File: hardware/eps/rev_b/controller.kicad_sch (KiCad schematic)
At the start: 11 parts, among them J100 SWD_ACCESS_LOGICAL, U100 STM32G0B1KET6N, Y100 ECS-3225MV-160-BN-TR

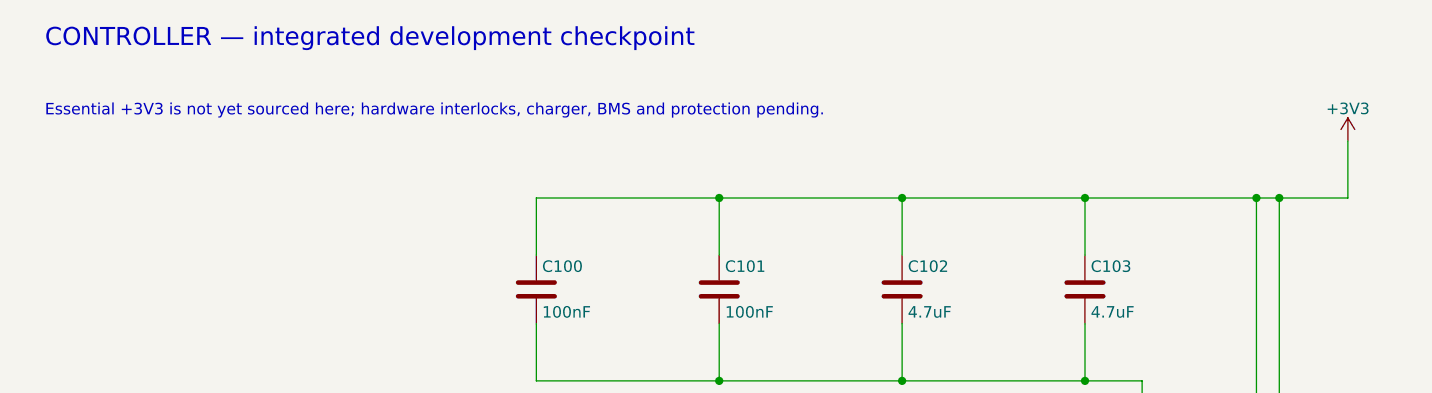
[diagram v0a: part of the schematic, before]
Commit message: Integrate essential 3V3 buck into EPS Rev B
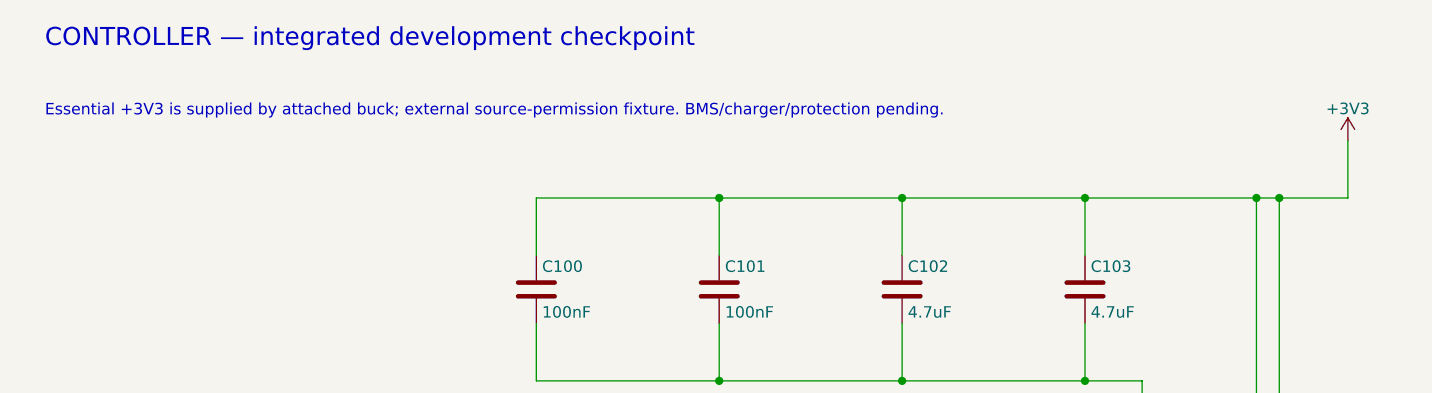
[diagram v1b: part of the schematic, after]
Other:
- note added: "Essential +3V3 is supplied by attached buck; external source-permission fixture. BMS/charger/protection pending."
- note removed: "Essential +3V3 is not yet sourced here; hardware interlocks, charger, BMS and protection pending."
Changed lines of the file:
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@@
     (effects (font (size 2 2)) (justify left bottom))
-  )
-  (text "Essential +3V3 is not yet sourced here; hardware interlocks, charger, BMS and protection pending."
-    (at 25.4 31.75 0)
-    (effects (font (size 1.27 1.27)) (justify left bottom))
   )
   (text "U100: STM32G0B1KET6N, N suffix. Pin 20 is VDDIO2, tied to VDD.\nPA11/PA12 allocation retained; USB/LSE unused. Verify UCPD reset configuration."
@@
     (effects (font (size 1.27 1.27)) (justify left bottom))
   )
+  (text "Essential +3V3 is supplied by attached buck; external source-permission fixture. BMS/charger/protection pending."
+    (at 25.4 31.75 0)
+    (effects (font (size 1.27 1.27)) (justify left bottom))
+  )

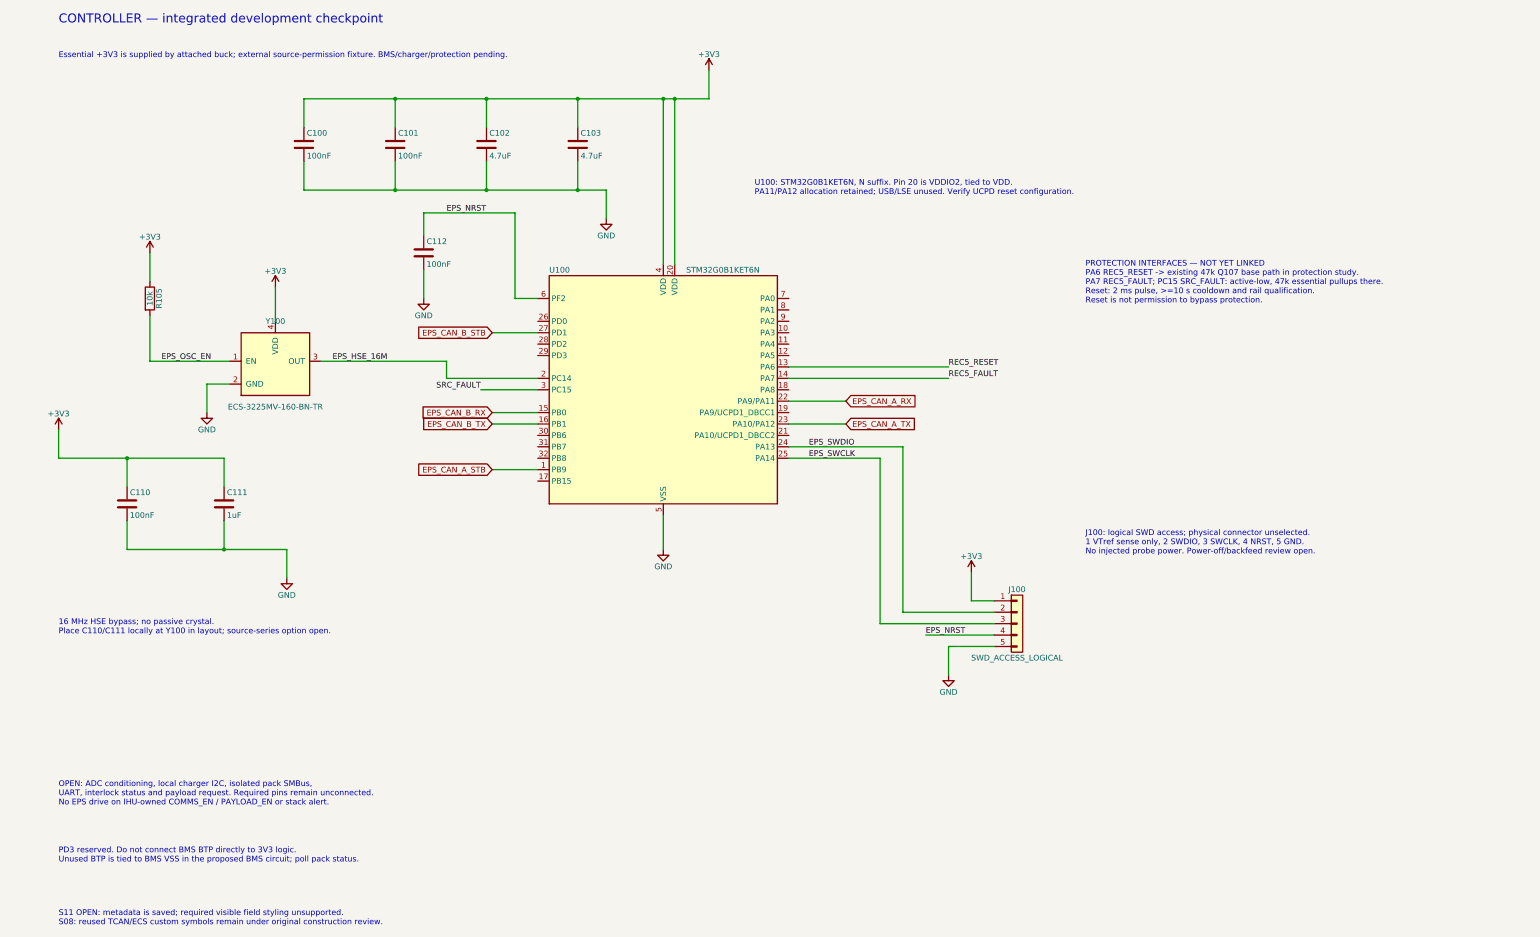
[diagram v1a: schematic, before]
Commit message: Integrate solar and recovery rail protection into EPS Rev B
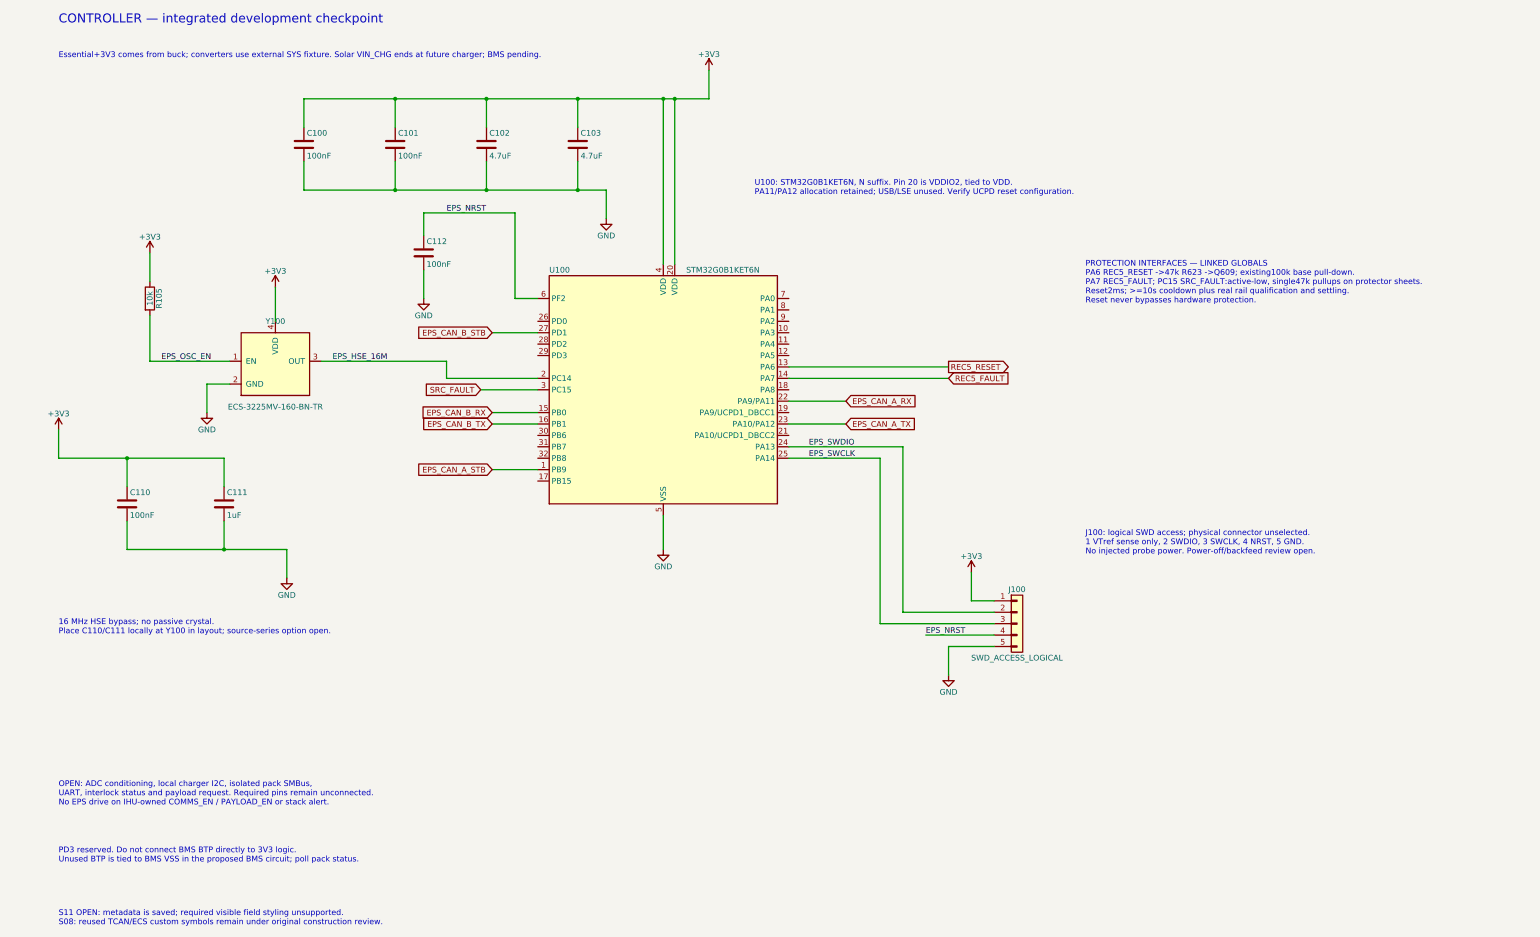
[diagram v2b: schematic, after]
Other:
- note added: "Essential+3V3 comes from buck; converters use external SYS fixture. Solar VIN_CHG ends at future charger; BMS pending."
- note added: "PROTECTION INTERFACES — LINKED GLOBALS PA6 REC5_RESET ->47k R623 ->Q609; existing100k base pull-down. PA7 REC5_FAULT; PC15 SRC_FAULT:active-low, single47k pullups on protector sheets. Reset2ms; >=10s cooldown plus real rail qualification and settling. Reset never bypasses hardware protection."
- note removed: "Essential +3V3 is supplied by attached buck; external source-permission fixture. BMS/charger/protection pending."
- note removed: "PROTECTION INTERFACES — NOT YET LINKED PA6 REC5_RESET -> existing 47k Q107 base path in protection study. PA7 REC5_FAULT; PC15 SRC_FAULT: active-low, 47k essential pullups there. Reset: 2 ms pulse, >=10 s cooldown and rail qualification. Reset is not permission to bypass protection."
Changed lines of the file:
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@@
+		)
+	)
+	(text "CONTROLLER — integrated development checkpoint"
+		(at 25.4 24.13 0)
+		(effects
+			(font
+				(size 2 2)
+			)
+			(justify left bottom)
+		)
+	)
+	(text "U100: STM32G0B1KET6N, N suffix. Pin 20 is VDDIO2, tied to VDD.\nPA11/PA12 allocation retained; USB/LSE unused. Verify UCPD reset configuration."
+		(at 180.34 62.23 0)
+		(effects
+			(font
+				(size 1.27 1.27)
+			)
+			(justify left bottom)
+		)
+	)
+	(text "J100: logical SWD access; physical connector unselected.\n1 VTref sense only, 2 SWDIO, 3 SWCLK, 4 NRST, 5 GND.\nNo injected probe power. Power-off/backfeed review open."
+		(at 254 142.24 0)
+		(effects
+			(font
+				(size 1.27 1.27)
+			)
+			(justify left bottom)
+		)
+	)
+	(text "16 MHz HSE bypass; no passive crystal.\nPlace C110/C111 locally at Y100 in layout; source-series option open."
+		(at 25.4 160.02 0)
+		(effects
+			(font
+				(size 1.27 1.27)
+			)
+			(justify left bottom)
+		)
+	)
+	(text "OPEN: ADC conditioning, local charger I2C, isolated pack SMBus,\nUART, interlock status and payload request. Required pins remain unconnected.\nNo EPS drive on IHU-owned COMMS_EN / PAYLOAD_EN or stack alert."
+		(at 25.4 198.12 0)
+		(effects
+			(font
+				(size 1.27 1.27)
+			)
+			(justify left bottom)
+		)
+	)
+	(text "PD3 reserved. Do not connect BMS BTP directly to 3V3 logic.\nUnused BTP is tied to BMS VSS in the proposed BMS circuit; poll pack status."
+		(at 25.4 210.82 0)
+		(effects
+			(font
+				(size 1.27 1.27)
+			)
+			(justify left bottom)
+		)
+	)
+	(text "S11 OPEN: metadata is saved; required visible field styling unsupported.\nS08: reused TCAN/ECS custom symbols remain under original construction review."
+		(at 25.4 224.79 0)
+		(effects
+			(font
+				(size 1.27 1.27)
+			)
+			(justify left bottom)
 		)
 	)
@@
 		)
 	)
-	(label "REC5_RESET"
+	(global_label "EPS_CAN_A_STB"
+		(shape input)
+		(at 121.92 123.19 180)
+		(effects
+			(font
+				(size 1.27 1.27)
+			)
+			(justify right)
+		)
+	)
+	(global_label "EPS_CAN_B_RX"
+		(shape input)
+		(at 121.92 110.49 180)
+		(effects
+			(font
+				(size 1.27 1.27)
+			)
+			(justify right)
+		)
+	)
+	(global_label "EPS_CAN_B_TX"
+		(shape input)
+		(at 121.92 113.03 180)
+		(effects
+			(font
+				(size 1.27 1.27)
+			)
+			(justify right)
+		)
+	)
+	(global_label "EPS_CAN_B_STB"
+		(shape input)
+		(at 121.92 92.71 180)
+		(effects
+			(font
+				(size 1.27 1.27)
+			)
+			(justify right)
+		)
+	)
+	(global_label "EPS_CAN_A_RX"
+		(shape input)
+		(at 200.66 107.95 0)
+		(effects
+			(font
+				(size 1.27 1.27)
+			)
+			(justify left)
+		)
+	)
+	(global_label "EPS_CAN_A_TX"
+		(shape input)
+		(at 200.66 113.03 0)
+		(effects
+			(font
+				(size 1.27 1.27)
+			)
+			(justify left)
+		)
+	)
+	(global_label "REC5_RESET"
+		(shape output)
 		(at 223.52 100.33 0)
 		(effects
@@
 				(size 1.27 1.27)
 			)
-			(justify left bottom)
-		)
-	)
-	(label "REC5_FAULT"
+			(justify left)
+		)
+	)
+	(global_label "REC5_FAULT"
+		(shape input)
 		(at 223.52 102.87 0)
 		(effects
@@
 				(size 1.27 1.27)
 			)
-			(justify left bottom)
-		)
-	)
-	(label "SRC_FAULT"
+			(justify left)
+		)
+	)
+	(global_label "SRC_FAULT"
+		(shape input)
 		(at 119.38 105.41 180)
 		(effects
@@
 				(size 1.27 1.27)
 			)
-			(justify right bottom)
-		)
-	)
-	(global_label "EPS_CAN_A_STB"
-		(shape input)
-		(at 121.92 123.19 180)
-		(effects
-			(font
-				(size 1.27 1.27)
-			)
-			(justify right)
-		)
-	)
-	(global_label "EPS_CAN_B_RX"
-		(shape input)
-		(at 121.92 110.49 180)
-		(effects
-			(font
-				(size 1.27 1.27)
-			)
-			(justify right)
-		)
-	)
-	(global_label "EPS_CAN_B_TX"
-		(shape input)
-		(at 121.92 113.03 180)
-		(effects
-			(font
-				(size 1.27 1.27)
-			)
-			(justify right)
-		)
-	)
-	(global_label "EPS_CAN_B_STB"
-		(shape input)
-		(at 121.92 92.71 180)
-		(effects
-			(font
-				(size 1.27 1.27)
-			)
-			(justify right)
-		)
-	)
-	(global_label "EPS_CAN_A_RX"
-		(shape input)
-		(at 200.66 107.95 0)
-		(effects
-			(font
-				(size 1.27 1.27)
-			)
-			(justify left)
-		)
-	)
-	(global_label "EPS_CAN_A_TX"
-		(shape input)
-		(at 200.66 113.03 0)
-		(effects
-			(font
-				(size 1.27 1.27)
-			)
-			(justify left)
-		)
-	)
-  (text "CONTROLLER — integrated development checkpoint"
-    (at 25.4 24.13 0)
-    (effects (font (size 2 2)) (justify left bottom))
-  )
-  (text "U100: STM32G0B1KET6N, N suffix. Pin 20 is VDDIO2, tied to VDD.\nPA11/PA12 allocation retained; USB/LSE unused. Verify UCPD reset configuration."
-    (at 180.34 62.23 0)
+			(justify right)
+		)
+	)
+  (text "Essential+3V3 comes from buck; converters use external SYS fixture. Solar VIN_CHG ends at future charger; BMS pending."
+    (at 25.4 31.75 0)
     (effects (font (size 1.27 1.27)) (justify left bottom))
   )
-  (text "PROTECTION INTERFACES — NOT YET LINKED\nPA6 REC5_RESET -> existing 47k Q107 base path in protection study.\nPA7 REC5_FAULT; PC15 SRC_FAULT: active-low, 47k essential pullups there.\nReset: 2 ms pulse, >=10 s cooldown and rail qualification.\nReset is not permission to bypass protection."
+  (text "PROTECTION INTERFACES — LINKED GLOBALS\nPA6 REC5_RESET ->47k R623 ->Q609; existing100k base pull-down.\nPA7 REC5_FAULT; PC15 SRC_FAULT:active-low, single47k pullups on protector sheets.\nReset2ms; >=10s cooldown plus real rail qualification and settling.\nReset never bypasses hardware protection."
     (at 254 86.36 0)
     (effects (font (size 1.27 1.27)) (justify left bottom))
   )
-  (text "J100: logical SWD access; physical connector unselected.\n1 VTref sense only, 2 SWDIO, 3 SWCLK, 4 NRST, 5 GND.\nNo injected probe power. Power-off/backfeed review open."
-    (at 254 142.24 0)
-    (effects (font (size 1.27 1.27)) (justify left bottom))
-  )
-  (text "16 MHz HSE bypass; no passive crystal.\nPlace C110/C111 locally at Y100 in layout; source-series option open."
-    (at 25.4 160.02 0)
-    (effects (font (size 1.27 1.27)) (justify left bottom))
-  )
-  (text "OPEN: ADC conditioning, local charger I2C, isolated pack SMBus,\nUART, interlock status and payload request. Required pins remain unconnected.\nNo EPS drive on IHU-owned COMMS_EN / PAYLOAD_EN or stack alert."
-    (at 25.4 198.12 0)
-    (effects (font (size 1.27 1.27)) (justify left bottom))
-  )
-  (text "PD3 reserved. Do not connect BMS BTP directly to 3V3 logic.\nUnused BTP is tied to BMS VSS in the proposed BMS circuit; poll pack status."
-    (at 25.4 210.82 0)
-    (effects (font (size 1.27 1.27)) (justify left bottom))
-  )
-  (text "S11 OPEN: metadata is saved; required visible field styling unsupported.\nS08: reused TCAN/ECS custom symbols remain under original construction review."
-    (at 25.4 224.79 0)
-    (effects (font (size 1.27 1.27)) (justify left bottom))
-  )
-  (text "Essential +3V3 is supplied by attached buck; external source-permission fixture. BMS/charger/protection pending."
-    (at 25.4 31.75 0)
-    (effects (font (size 1.27 1.27)) (justify left bottom))
-  )

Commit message: Integrate LTC4162 charger PowerPath and thermistor interface into EPS Rev B
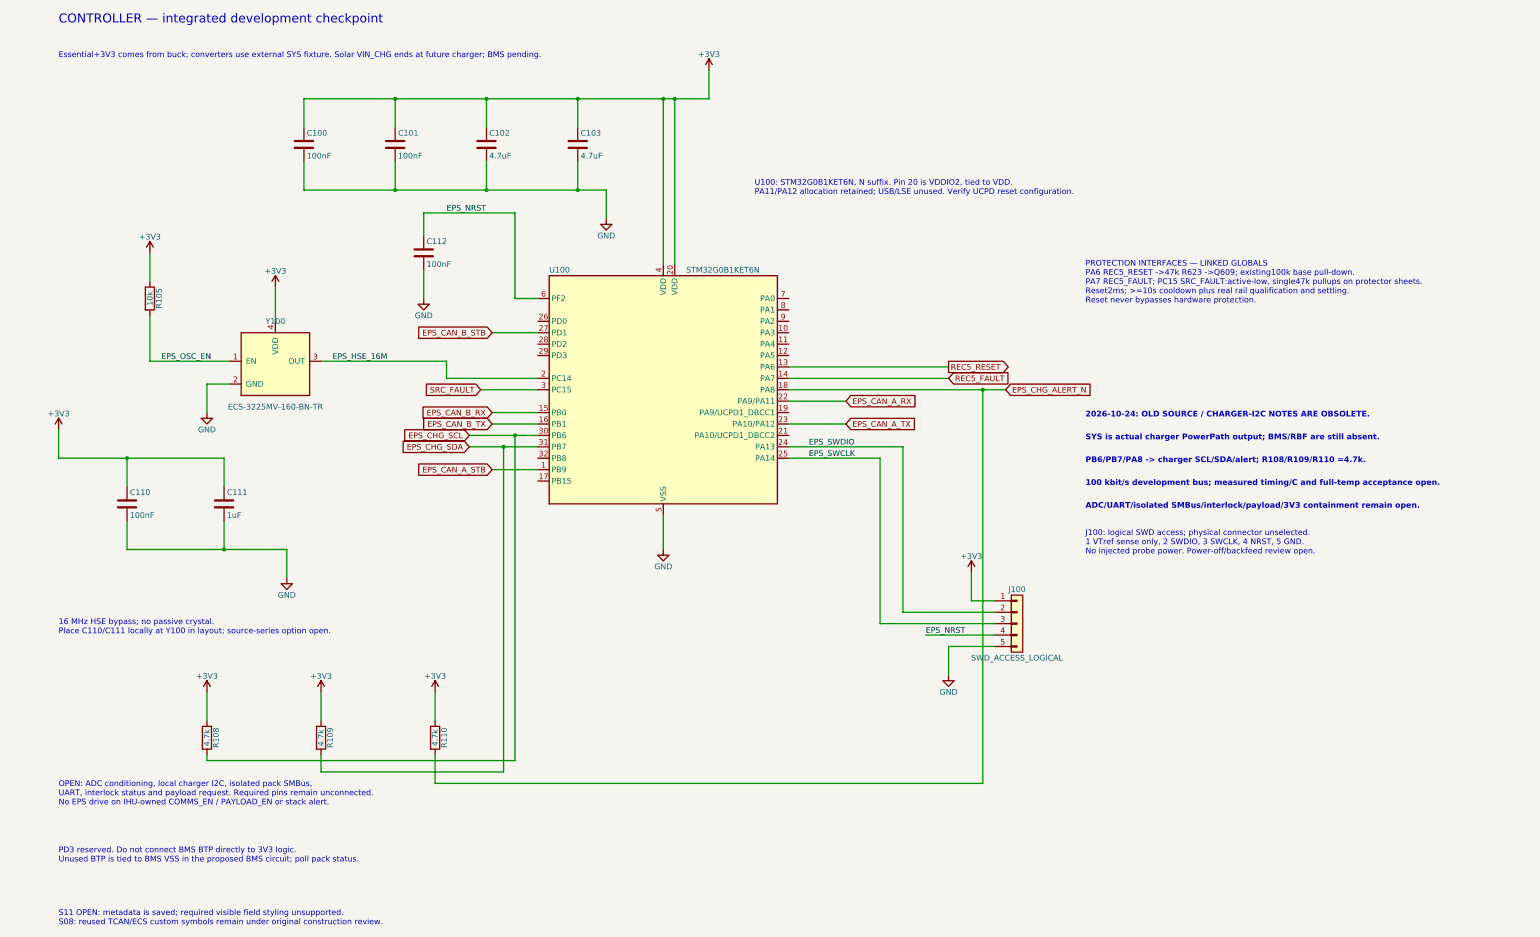
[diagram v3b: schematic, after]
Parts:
- added R108, R109, R110: 4.7k, Resistor_SMD:R_0603_1608Metric, symbol Device:R
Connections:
- net +3V3: now also R108.1, R109.1, R110.1
- net EPS_CHG_ALERT_N: now reaches U100.18 (PA8)
- net EPS_CHG_ALERT_N: now also R110.2
- net EPS_CHG_SCL: now reaches U100.30 (PB6)
- net EPS_CHG_SCL: now also R108.2
- net EPS_CHG_SDA: now reaches U100.31 (PB7)
- net EPS_CHG_SDA: now also R109.2
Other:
- note added: "100 kbit/s development bus; measured timing/C and full-temp acceptance open."
- note added: "2026-10-24: OLD SOURCE / CHARGER-I2C NOTES ARE OBSOLETE."
- note added: "ADC/UART/isolated SMBus/interlock/payload/3V3 containment remain open."
- note added: "PB6/PB7/PA8 -> charger SCL/SDA/alert; R108/R109/R110 =4.7k."
- note added: "SYS is actual charger PowerPath output; BMS/RBF are still absent."
